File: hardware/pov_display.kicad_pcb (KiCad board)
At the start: 2 copper layers, 40 x 100 mm, 36 parts, among them J1 Conn_01x01_Male, J2 Conn_01x01_Male, J3 Conn_01x01_Male, J4 Conn_01x01_Male, J5 Conn_01x01_Male, J6 Conn_01x06_Male, U1 PIC16F676-IP, U2 LM7805_TO220

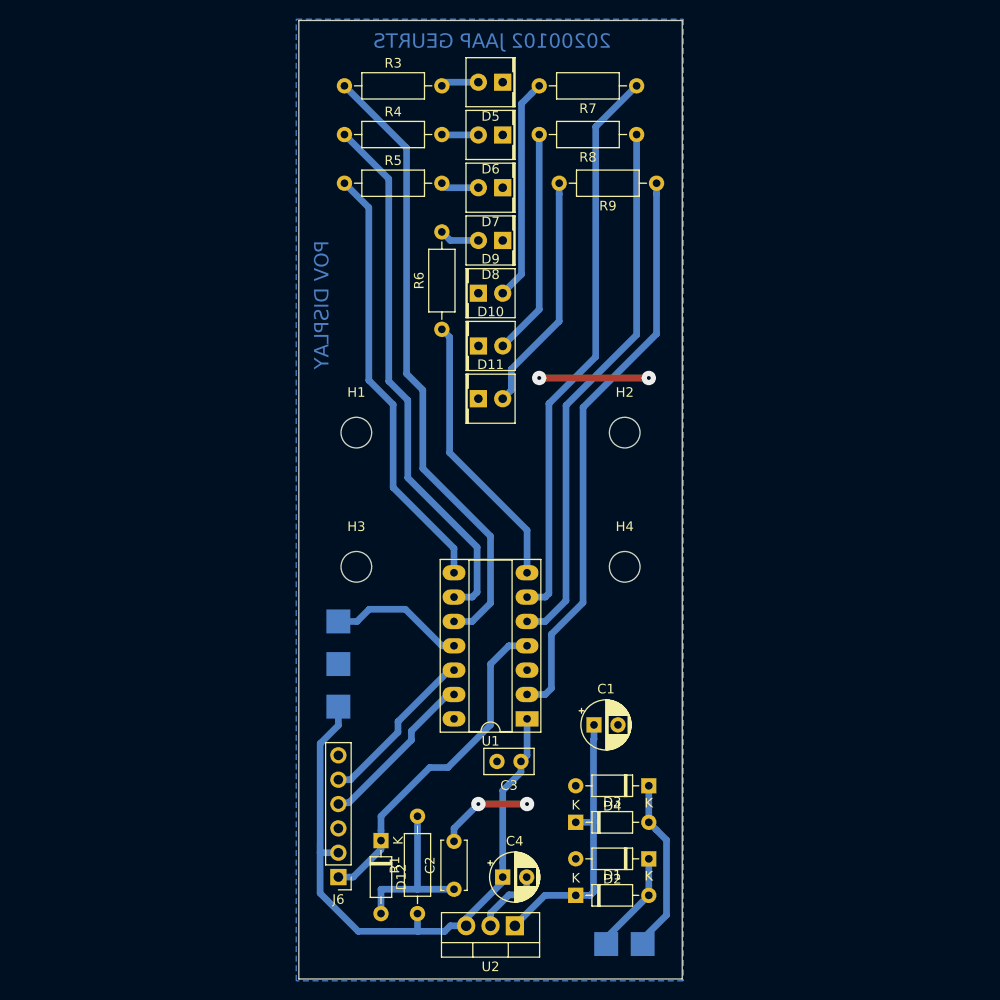
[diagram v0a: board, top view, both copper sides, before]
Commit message: Cosmetic updates, removed unwanted files
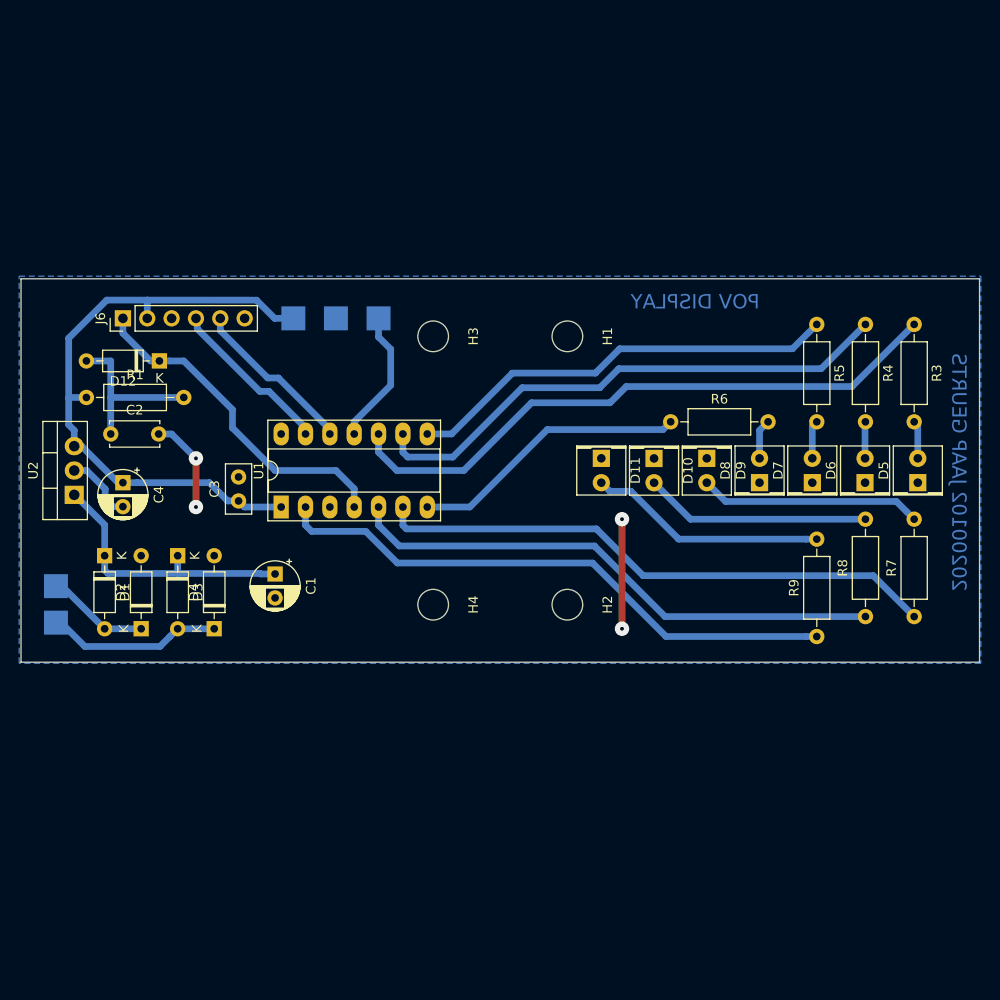
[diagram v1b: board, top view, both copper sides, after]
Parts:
- moved J2 69.8 mm to (84.7, 117.8), turned to 270 degrees
- moved J1 68.5 mm to (84.7, 114.0), turned to 270 degrees
- moved R3 64.4 mm to (174.2, 86.7), turned to 270 degrees
- moved U2 64.3 mm to (86.6, 104.5), turned to 90 degrees
- moved R1 64.0 mm to (87.8, 94.3), turned to 0 degrees
- moved R7 62.5 mm to (174.2, 117.2), turned to 90 degrees
- moved J6 62.5 mm to (91.6, 86.1), turned to 90 degrees
- moved D1 60.6 mm to (89.7, 110.8), turned to 270 degrees
- moved D5 60.2 mm to (174.6, 103.2), turned to 90 degrees
- moved C2 59.5 mm to (90.4, 98.1), turned to 0 degrees
- moved D2 58.1 mm to (93.6, 118.5), turned to 90 degrees
- moved R4 57.9 mm to (169.1, 86.7), turned to 270 degrees
- moved C4 57.1 mm to (91.6, 103.2), turned to 270 degrees
- moved R8 55.7 mm to (169.1, 117.2), turned to 90 degrees
- moved D12 55.1 mm to (95.5, 90.5), turned to 180 degrees
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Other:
- board size 40 x 100 mm -> 100 x 40 mm
